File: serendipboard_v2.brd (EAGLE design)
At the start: 38.1 x 66.3 mm, 85 parts, among them IC1 TP4056, IC2 DW01A, IC3 DS3231/SO, J4 USB3076-XX-X_REVC, Q1 FS8205A, Q2 MMBT2222ALT1G, Q3 RUC002N05HZGT116, Q4 DMG3415U, Q5 MMBT2222ALT1G, Q7 RUC002N05HZGT116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

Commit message: .
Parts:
- moved R5 6.98 mm to (6.35, 22.9)
- moved R3 6.54 mm to (10.8, 8.26)
- moved C5 4.45 mm to (6.35, 24.1), turned to 0 degrees
- moved U7 4.45 mm to (6.35, 28.6)
- moved C23 2.01 mm to (25.4, 6.35)
- moved C22 2.01 mm to (25.4, 5.08)
- moved C24 2.01 mm to (25.4, 7.62)
- moved C4 2.01 mm to (5.08, 4.45), turned to 180 degrees
- moved R4 2.01 mm to (5.08, 3.17), turned to 0 degrees
- moved C21 1.91 mm to (6.35, 25.4)
- moved R1 1.91 mm to (13.3, 14.0), turned to 90 degrees
- moved R17 1.27 mm to (13.3, 20.3), turned to 270 degrees
- moved R18 1.27 mm to (12.1, 20.3), turned to 90 degrees
- moved R22 1.27 mm to (27.3, 12.7), turned to 180 degrees
- moved R23 1.27 mm to (27.3, 11.4), turned to 0 degrees
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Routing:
- net GND: track 17.1 -> 134.8 mm, vias 0 -> 17
- net VBUS: track 0.00 -> 57.8 mm, vias 0 -> 5
- net VBAT: track 0.00 -> 53.4 mm, vias 0 -> 6
- net N$2: track 0.00 -> 18.5 mm
- net VIN: track 0.00 -> 18.2 mm
- net B-: track 0.65 -> 15.2 mm, vias 0 -> 1
- net 1.8V: track 0.07 -> 12.4 mm
- net N$4: track 0.00 -> 12.0 mm
- net N$3: track 0.00 -> 11.5 mm, vias 0 -> 3
- net N$9: track 0.00 -> 9.17 mm, vias 0 -> 1
- net IO0: track 0.00 -> 8.51 mm
- net 3V3OUT: track 0.00 -> 8.14 mm, vias 0 -> 2
- net SHIELD: track 0.00 -> 7.70 mm
- net N$1: track 0.00 -> 7.50 mm
- net N$21: track 0.00 -> 7.37 mm
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- added copper zone on layer 16, net GND
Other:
- board size 38.1 x 66.3 mm -> 38.1 x 60.6 mm

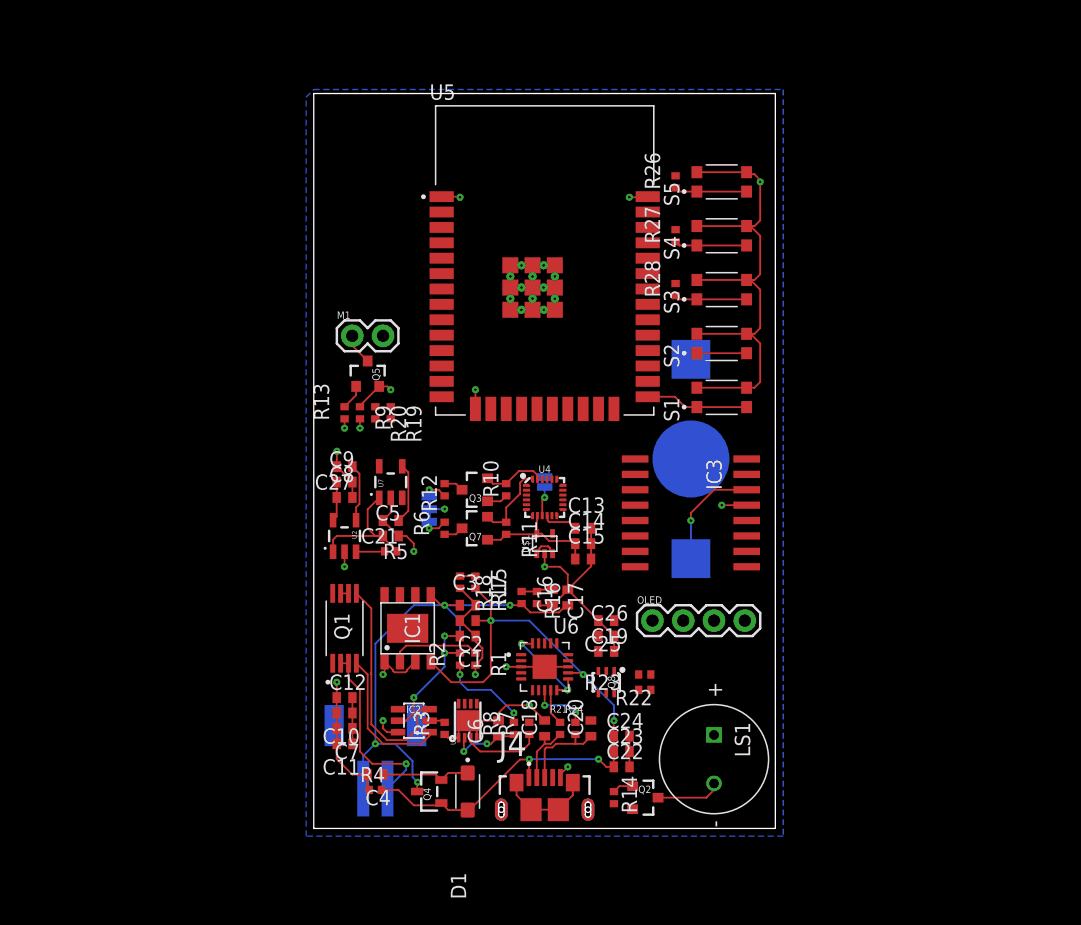
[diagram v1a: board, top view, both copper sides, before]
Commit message: Update serendipboard_v2.brd
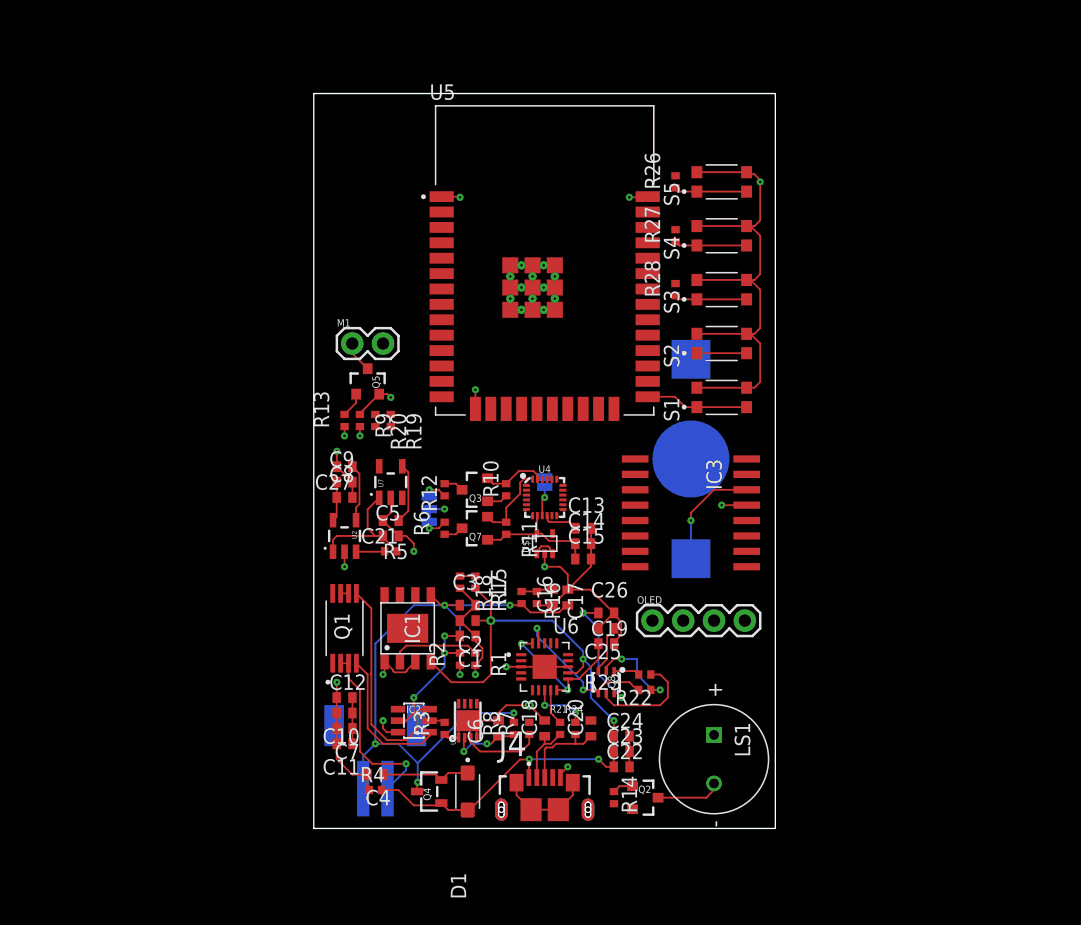
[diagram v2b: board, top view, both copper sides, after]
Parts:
- moved C26 1.91 mm to (24.1, 17.8)
- moved Q5 0.64 mm to (4.45, 36.8)
- moved C19 0.63 mm to (24.1, 15.2)
- moved C25 0.63 mm to (24.1, 16.5)
- moved M1 0.63 mm to (3.17, 40.0)
- moved R13 0.63 mm to (2.54, 33.7)
- moved R19 0.63 mm to (6.35, 33.7)
- moved R20 0.63 mm to (5.08, 33.7)
- moved R9 0.63 mm to (3.81, 33.7)
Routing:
- net RTS: track 0.00 -> 13.5 mm, vias 0 -> 2
- net IO0: track 8.51 -> 18.8 mm, vias 0 -> 2
- net N$15: track 0.00 -> 8.89 mm
- net N$18: track 0.00 -> 7.62 mm, vias 0 -> 2
- net 3V3OUT: track 8.14 -> 12.6 mm
- net EN: track 4.10 -> 8.18 mm
- net VBAT: track 53.4 -> 57.0 mm
- net GND: track 134.8 -> 137.5 mm
- net DTR: track 0.00 -> 2.14 mm
- net VBUS: track 57.8 -> 59.7 mm
- removed copper zone on layer 16, net GND

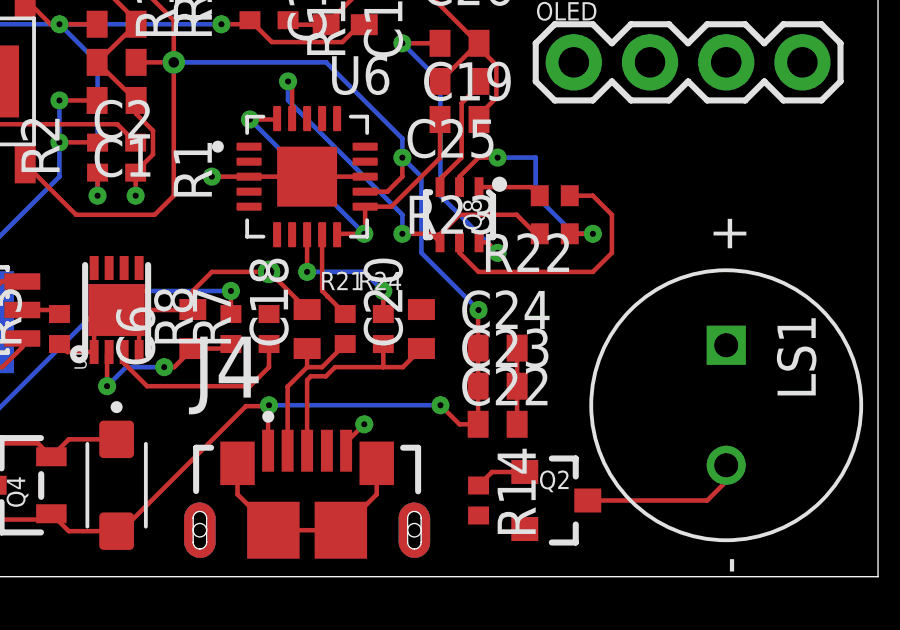
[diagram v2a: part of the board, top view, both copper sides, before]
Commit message: Update serendipboard_v2.brd
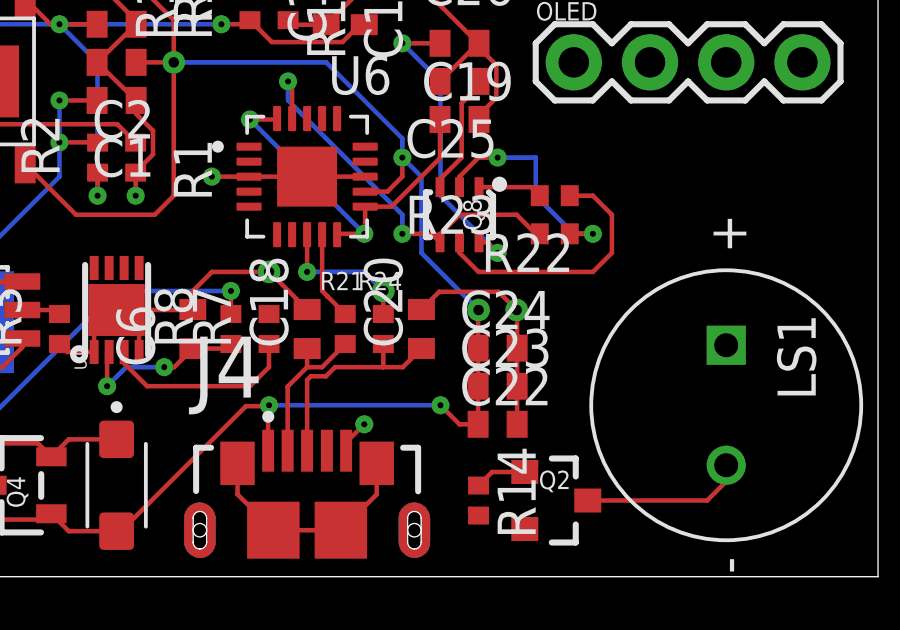
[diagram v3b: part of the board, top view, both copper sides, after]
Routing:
- net GND: track 137.5 -> 142.5 mm, vias 17 -> 18
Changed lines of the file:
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@@
 <wire x1="20.955" y1="19.7" x2="22.83" y2="19.7" width="0.1524" layer="1"/>
 <via x="17.78" y="10.16" extent="1-16" drill="0.35"/>
+<wire x1="26.05" y1="8.875" x2="26.05" y2="7.62" width="0.1524" layer="1"/>
+<wire x1="26.035" y1="8.89" x2="26.05" y2="8.875" width="0.1524" layer="1"/>
+<via x="26.035" y="8.89" extent="1-16" drill="0.35"/>
+<wire x1="26.035" y1="8.89" x2="25.4282" y2="9.4968" width="0.1524" layer="1"/>
+<wire x1="25.4282" y1="9.4968" x2="23.4518" y2="9.4968" width="0.1524" layer="1"/>
+<wire x1="23.4518" y1="9.4968" x2="22.86" y2="8.905" width="0.1524" layer="1"/>
 <wire x1="31.605" y1="54.14" x2="27.55" y2="52.123" width="0" layer="19" extent="1-1"/>
 <wire x1="31.115" y1="30.48" x2="31.605" y2="36.36" width="0" layer="19" extent="1-16"/>
@@
 <wire x1="17.78" y1="10.16" x2="17.115" y2="13.335" width="0" layer="19" extent="1-1"/>
 <wire x1="22.86" y1="8.905" x2="19.05" y2="8.905" width="0" layer="19" extent="1-1"/>
-<wire x1="26.05" y1="7.62" x2="22.86" y2="8.905" width="0" layer="19" extent="1-1"/>
 <wire x1="26.305" y1="1.59" x2="26.05" y2="5.08" width="0" layer="19" extent="1-1"/>
 <wire x1="6.955" y1="7.94" x2="10.795" y2="7.755" width="0" layer="19" extent="1-1"/>
@@
 <via x="22.225" y="13.97" extent="1-16" drill="0.2"/>
 <wire x1="24.75" y1="7.62" x2="24.75" y2="8.875" width="0.1524" layer="1"/>
-<wire x1="24.75" y1="8.875" x2="24.765" y2="8.89" width="0.1524" layer="1"/>
-<via x="24.765" y="8.89" extent="1-16" drill="0.2"/>
 <wire x1="22.225" y1="13.97" x2="22.86" y2="13.335" width="0.1524" layer="16"/>
 <wire x1="22.86" y1="13.335" x2="22.86" y2="10.795" width="0.1524" layer="16"/>
@@
 <wire x1="8.255" y1="1.905" x2="6.985" y2="3.175" width="0.1524" layer="1"/>
 <wire x1="6.985" y1="3.175" x2="5.58" y2="3.175" width="0.1524" layer="1"/>
+<via x="24.765" y="8.89" extent="1-16" drill="0.35"/>
+<wire x1="24.75" y1="8.875" x2="24.765" y2="8.89" width="0" layer="19" extent="1-1"/>
 </signal>
 <signal name="N$19">
@@
 <wire x1="19.05" y1="11.4" x2="19.05" y2="10.16" width="0.1524" layer="1"/>
 <via x="19.05" y="10.16" extent="1-16" drill="0.2"/>
-<via x="21.59" y="9.525" extent="1-16" drill="0.2"/>
 <wire x1="21.59" y1="9.525" x2="21.59" y2="8.755" width="0.1524" layer="1"/>
 <wire x1="19.05" y1="10.16" x2="20.955" y2="10.16" width="0.1524" layer="16"/>
 <wire x1="20.955" y1="10.16" x2="21.59" y2="9.525" width="0.1524" layer="16"/>
+<via x="21.59" y="9.525" extent="1-16" drill="0.35"/>
 </signal>
 <signal name="TXD">

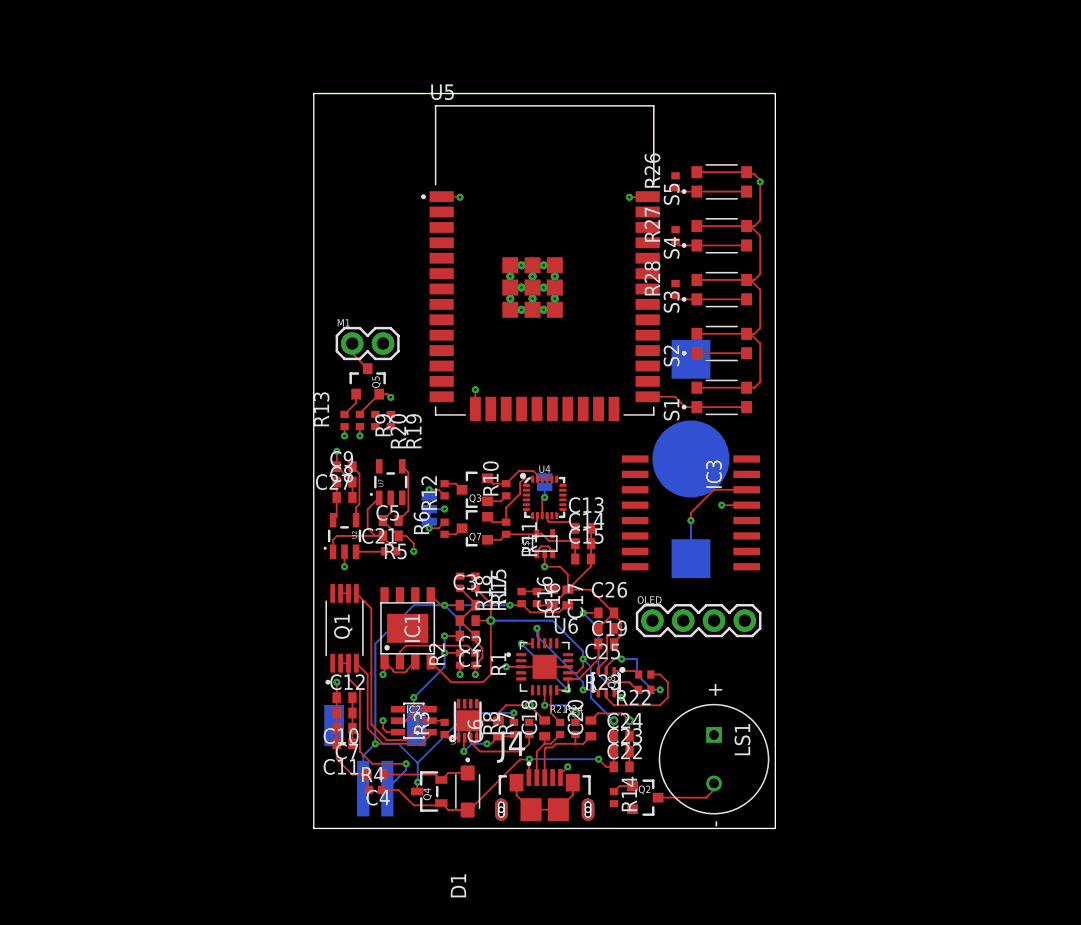
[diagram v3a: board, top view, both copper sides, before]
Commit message: Update serendipboard_v2.brd
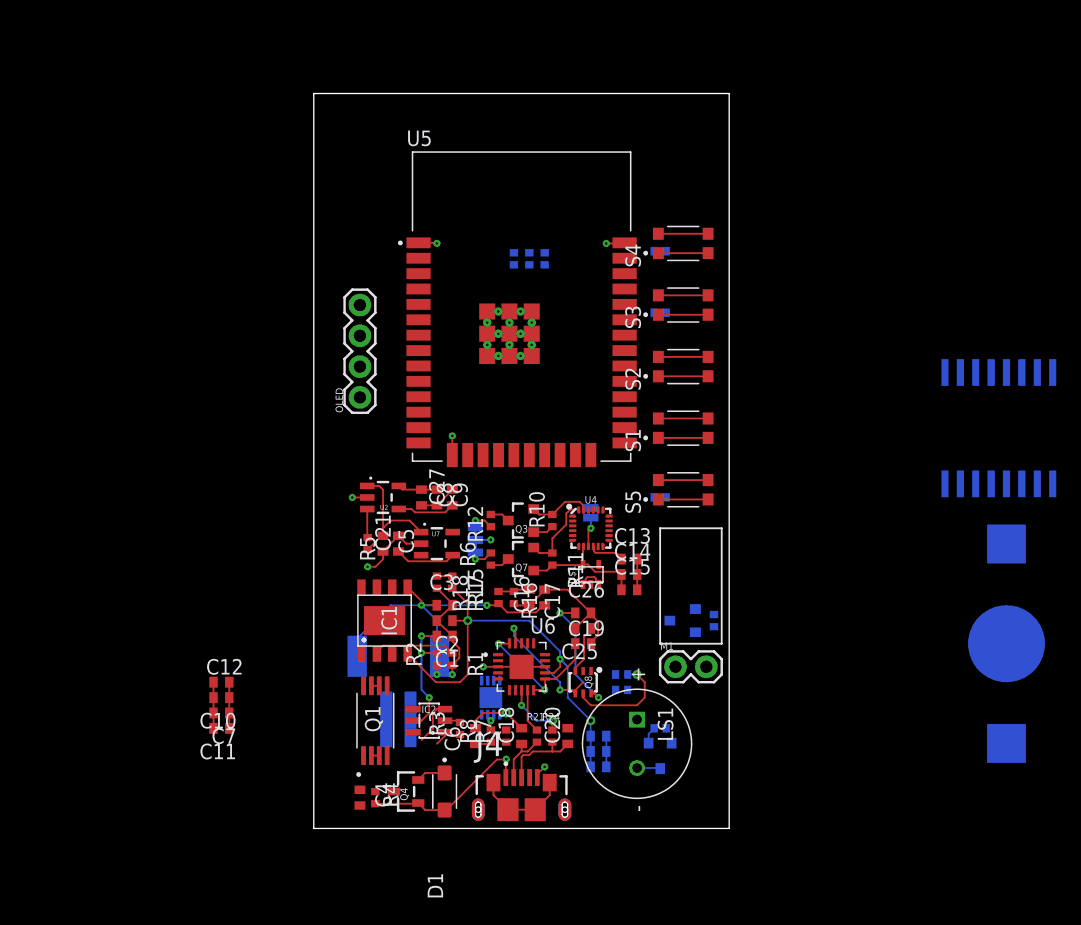
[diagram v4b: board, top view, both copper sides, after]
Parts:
- moved M1 37.7 mm to (29.8, 13.3)
- moved R13 34.7 mm to (33.0, 17.1), flipped to the bottom, turned to 270 degrees
- moved Q5 32.6 mm to (30.5, 17.1), flipped to the bottom, turned to 270 degrees
- moved OLED 30.4 mm to (3.81, 35.6), turned to 90 degrees
- moved B1 30.2 mm to (57.1, 15.2)
- moved IC3 26.3 mm to (56.5, 33.0), flipped to the bottom, turned to 180 degrees
- moved R26 26.1 mm to (28.6, 27.3), flipped to the bottom, turned to 180 degrees
- moved S5 25.6 mm to (30.5, 27.9)
- moved R9 20.3 mm to (19.1, 47.0), flipped to the bottom
- moved R20 18.4 mm to (17.8, 47.0), flipped to the bottom, turned to 90 degrees
- moved R19 16.8 mm to (16.5, 47.0), flipped to the bottom, turned to 90 degrees
- moved C10 10.2 mm to (-7.62, 10.8)
- moved C11 10.2 mm to (-7.62, 8.26)
- moved C12 10.2 mm to (-7.62, 12.1)
- moved C7 10.2 mm to (-7.62, 9.53)
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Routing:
- net GND: track 142.5 -> 80.1 mm, vias 18 -> 9
- net VBAT: track 57.0 -> 31.7 mm, vias 6 -> 4
- net N$2: track 18.5 -> 3.75 mm
- net B-: track 15.2 -> 0.65 mm, vias 1 -> 0
- net N$4: track 12.0 -> 1.23 mm
- net N$9: track 9.17 -> 0.00 mm, vias 1 -> 0
- net VBUS: track 59.7 -> 50.9 mm, vias 5 -> 4
- net N$18: track 7.62 -> 0.00 mm, vias 2 -> 0
- net N$6: track 6.55 -> 0.00 mm
- net VIN: track 18.2 -> 13.2 mm
- net N$7: track 5.88 -> 1.33 mm, vias 2 -> 0
- net IO0: track 18.8 -> 14.4 mm
- net N$19: track 5.42 -> 2.03 mm
- net RTS: track 13.5 -> 10.7 mm
- net N$17: track 2.60 -> 0.00 mm
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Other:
- board size 38.1 x 60.6 mm -> 34.3 x 60.6 mm

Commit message: .
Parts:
- added BATT1: (no value), SparkFun-Connectors:JST-2-SMD
- BATT: device SparkFun-Connectors:JST-2-SMD -> SparkFun-Connectors:1X02
- moved IC3 30.1 mm to (27.9, 23.5), turned to 0 degrees
- moved C16 27.5 mm to (-8.26, 22.2)
- moved C17 27.5 mm to (-9.53, 22.2)
- moved R15 27.5 mm to (-12.1, 22.2)
- moved R16 27.5 mm to (-10.8, 22.2)
- moved R17 22.3 mm to (-10.8, 19.1)
- moved R18 22.3 mm to (-12.1, 19.1)
- moved C26 7.65 mm to (27.3, 12.1), turned to 270 degrees
- moved BATT 7.65 mm to (1.91, 6.99), flipped to the top, turned to 90 degrees
- moved C25 5.85 mm to (26.0, 12.1), turned to 90 degrees
- moved C13 5.12 mm to (26.7, 17.1), turned to 270 degrees
- moved C19 4.07 mm to (24.8, 12.1), turned to 270 degrees
- moved C14 3.86 mm to (25.4, 17.1), turned to 270 degrees
- moved U$1 3.86 mm to (22.2, 17.1)
- moved JP1 3.81 mm to (13.3, 20.0)
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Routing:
- net VBAT: track 31.7 -> 9.87 mm, vias 4 -> 2
- net VBUS: track 50.9 -> 37.3 mm
- net GND: track 80.1 -> 68.7 mm, vias 9 -> 8
- net N$15: track 8.89 -> 0.35 mm, vias 1 -> 0
- net N$1: track 6.86 -> 0.00 mm
- net IO0: track 14.4 -> 8.81 mm
- net N$3: track 10.7 -> 5.36 mm
- net EN: track 8.18 -> 4.53 mm
- net 3V3OUT: track 12.6 -> 9.02 mm
- net BATT_MONITOR: track 2.60 -> 0.21 mm
- net N$11: track 2.96 -> 4.94 mm
- net 1.8V: track 12.4 -> 11.4 mm
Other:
- board size 34.3 x 60.6 mm -> 34.3 x 56.8 mm
